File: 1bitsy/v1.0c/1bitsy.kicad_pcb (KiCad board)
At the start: 4 copper layers, 38.1 x 17.8 mm, 105 parts, among them J1 BOOT, P1 CONN_01X01, P10 CONN_01X01, P11 CONN_01X01, P12 CONN_01X01, P13 CONN_01X01, P14 CONN_01X01, P15 CONN_01X01, P16 CONN_01X01, P17 CONN_01X01, P18 CONN_01X01, P19 CONN_01X01, P2 CONN_01X01, P20 CONN_01X01, P21 CONN_01X01, P22 CONN_01X01, P23 CONN_01X01, P24 USB_OTG, P25 CONN_01X01, P26 CONN_01X01, P27 CONN_01X01, P28 CONN_01X01, P29 CONN_01X01, P3 CONN_01X01, P30 CONN_01X01, P31 CONN_01X01, P32 CONN_01X01, P33 CONN_01X01, P34 CONN_01X01, P35 CONN_01X01, P36 CONN_01X01, P37 CONN_01X01, P38 CONN_01X01, P39 CONN_01X01, P4 CONN_01X01, P40 CONN_01X01, P41 CONN_01X01, P42 CONN_01X01, P43 TP, P44 TP, P45 TP, P46 TP, P47 TP, P48 CONN_01X01, P49 CONN_01X01, P5 CONN_01X01, P50 CONN_01X01, P51 CONN_01X01, P52 CONN_01X01, P53 CONN_01X01, P54 CONN_01X01, P55 CONN_01X01, P6 CONN_01X01, P7 CONN_01X01, P8 CONN_01X01, P9 CONN_01X01, SW1 TACT_G, U1 VREG_3V3, U2 STM32F415RGT, X1 32.768kHz, X2 25MHz, X3 JTAG-10

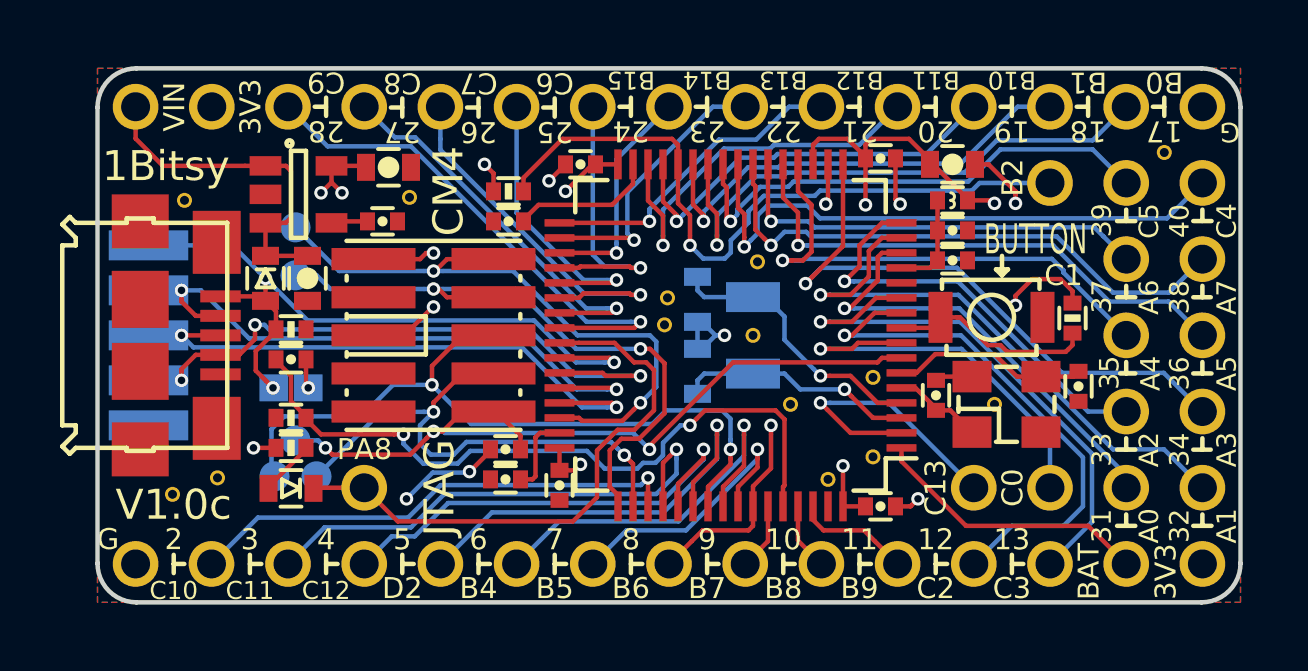
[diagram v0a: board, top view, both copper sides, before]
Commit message: More silkscreen polish.
Made the pixelheart larger, moved some via away from silkscreen lines.
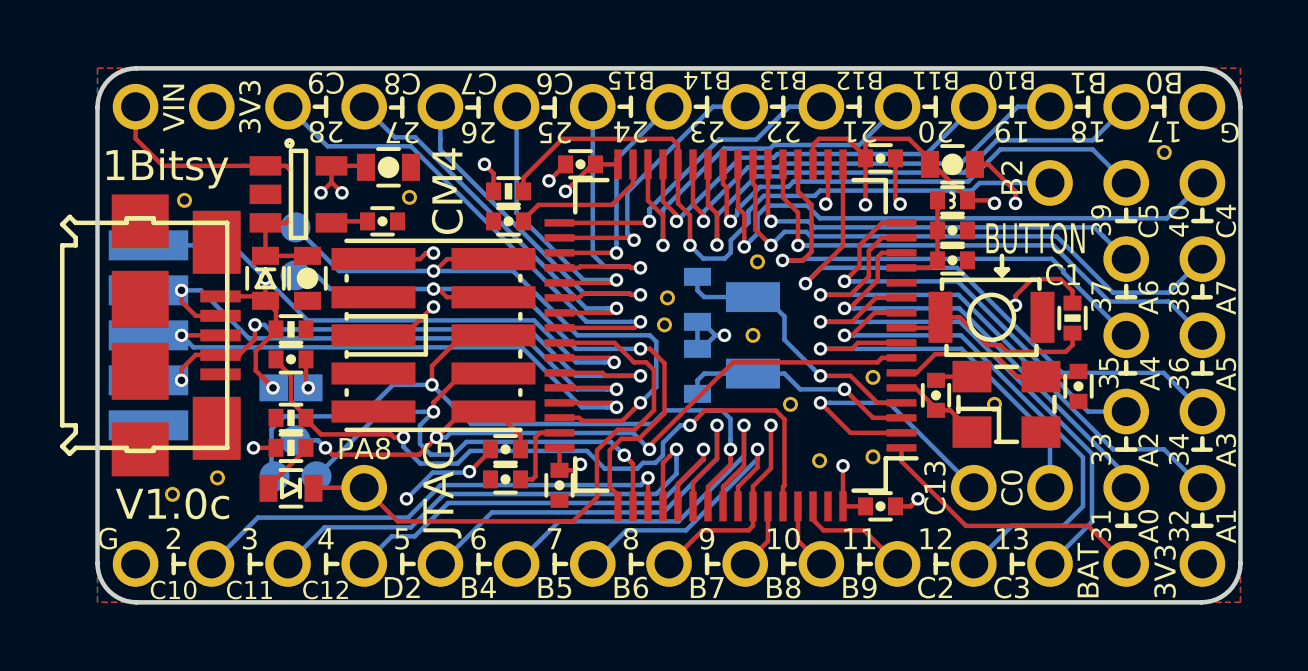
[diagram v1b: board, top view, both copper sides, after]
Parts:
- REF**: footprint pkl_logos:heart_mask_010grid -> pkl_logos:heart_mask_015grid
- moved REF** 0.76 mm to (130.0, 48.9)
- moved REF** 0.68 mm to (124.4, 49.9)

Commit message: Removed serial pin numbering, left only pin bank+pin no.
We got rid of the pcb specific numbering to make space for larger
internal mcu numbering labels. These are much more important when
writing code for the board.
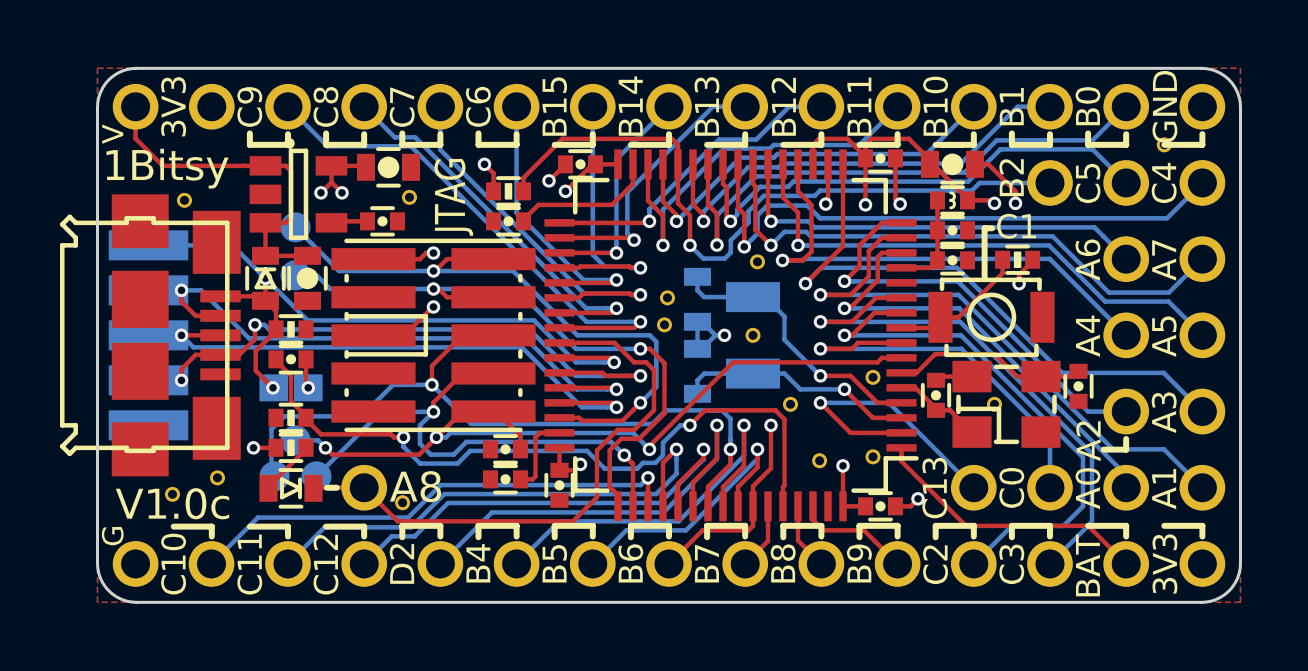
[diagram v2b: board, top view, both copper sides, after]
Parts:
- added REF**: via0305, pkl_misc:via0305, F.Cu at (110.5, 51.3)
- moved R5 2.67 mm to (131.0, 43.2), turned to 180 degrees
- moved REF** 0.78 mm to (127.1, 45.7)
- moved REF** 0.25 mm to (135.9, 39.4)
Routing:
- net GND: track 18.8 -> 15.3 mm, vias 10 -> 8
- net /BUTTON: track 6.81 -> 4.57 mm
- net +3V3: track 24.5 -> 22.5 mm
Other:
- board text added: "A8"
- board text added: "V"
- board text removed: "31"
- board text removed: "32"
- board text removed: "33"
- board text removed: "34"
- board text removed: "35"
- board text removed: "36"
- board text removed: "37"
- board text removed: "38"
- board text removed: "39"
- board text removed: "40"
- board text removed: "BUTTON"
- board text removed: "CM4"
- board text removed: "PA8"

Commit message: Some more Silkscreen cleanup work.
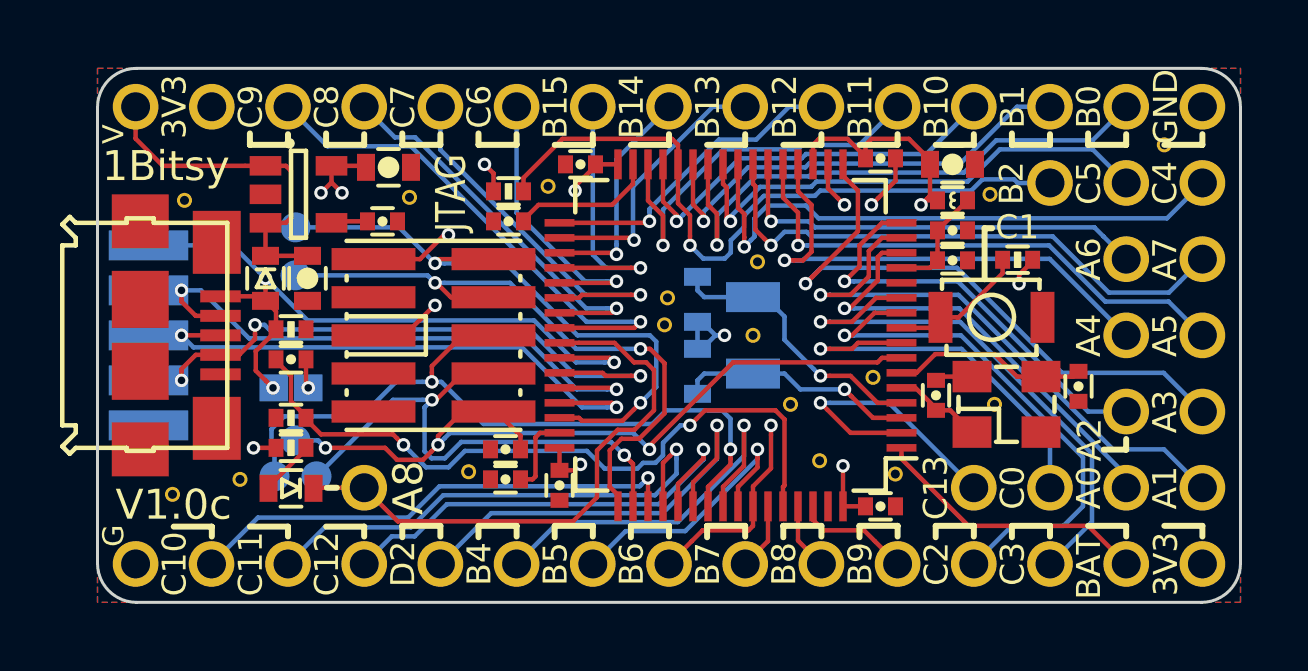
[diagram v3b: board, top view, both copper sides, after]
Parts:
- removed LOGO1: 1BitSquared, pkl_logos:1b2_Logo_SilkS_7.5mm
- added REF**: via0305, pkl_misc:via0305, F.Cu at (115.3, 40.8)
- added REF**: via0305, pkl_misc:via0305, F.Cu at (130.1, 41.0)
- added REF**: 1b2_Logo_SilkS_6.5mm, pkl_logos:1b2_Logo_SilkS_6.5mm, B.Cu at (111.9, 45.7)
- moved REF** 2.43 mm to (112.7, 50.3)
- moved REF** 0.94 mm to (126.9, 50.3)
- moved REF** 0.75 mm to (105.1, 50.5)
- moved REF** 0.30 mm to (129.7, 48.9)
- turned L1 to 0 degrees
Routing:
- net GND: track 15.3 -> 12.2 mm, vias 8 -> 5
- net +3V3: track 22.5 -> 20.8 mm, vias 10 -> 9
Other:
- board text added: "OSHPark"
- board text added: "with by"
- board text removed: "with by OSHPark"

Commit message: Swapped C4 & C5 for consistency.
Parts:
- moved P14 2.54 mm to (134.6, 40.6)
- moved P15 2.54 mm to (137.2, 40.6)
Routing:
- net /PC4: track 19.7 -> 17.2 mm
- net /PC5: track 16.7 -> 19.3 mm
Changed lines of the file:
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@@
     (thickness 1.6)
     (drawings 336)
-    (tracks 738)
+    (tracks 739)
     (zones 0)
     (modules 108)
@@
   )
   (module pkl_pin_headers:Pin_Header_Straight_Round_1x01 (layer F.Cu)
-    (at 137.16 40.64)
+    (at 134.62 40.64)
     (descr "Through hole pin header")
     (tags "pin header")
@@
   )
   (module pkl_pin_headers:Pin_Header_Straight_Round_1x01 (layer F.Cu)
-    (at 134.62 40.64 180)
+    (at 137.16 40.64 180)
     (descr "Through hole pin header")
     (tags "pin header")
@@
     (effects (font (size 0.8 0.8) (thickness 0.2)) (justify mirror))
   )
-  (gr_text C4 (at 135.9154 40.64 90) (layer B.SilkS)
+  (gr_text C4 (at 133.3754 40.64 90) (layer B.SilkS)
     (effects (font (size 0.8 0.8) (thickness 0.2)) (justify mirror))
   )
-  (gr_text C5 (at 133.3754 40.64 90) (layer B.SilkS)
+  (gr_text C5 (at 135.9408 40.64 90) (layer B.SilkS)
     (effects (font (size 0.8 0.8) (thickness 0.2)) (justify mirror))
   )
@@
     (effects (font (size 0.8 0.8) (thickness 0.2)))
   )
-  (gr_text C4 (at 135.9154 40.64 90) (layer F.SilkS)
+  (gr_text C4 (at 133.3754 40.64 90) (layer F.SilkS)
     (effects (font (size 0.8 0.8) (thickness 0.2)))
   )
-  (gr_text C5 (at 133.3754 40.64 90) (layer F.SilkS)
+  (gr_text C5 (at 135.9408 40.64 90) (layer F.SilkS)
     (effects (font (size 0.8 0.8) (thickness 0.2)))
   )
@@
   (segment (start 124.748198 45.27) (end 124.43 45.27) (width 0.15) (layer B.Cu) (net 27))
   (via (at 124.43 45.27) (size 0.45) (drill 0.25) (layers F.Cu B.Cu) (net 27))
-  (segment (start 137.16 40.64) (end 135.980999 41.819001) (width 0.15) (layer B.Cu) (net 28))
-  (segment (start 135.980999 41.819001) (end 124.364479 41.819001) (width 0.15) (layer B.Cu) (net 28))
-  (segment (start 124.364479 41.819001) (end 123.940478 41.395) (width 0.15) (layer B.Cu) (net 28))
-  (segment (start 123.940478 41.395) (end 122.655 41.395) (width 0.15) (layer B.Cu) (net 28))
-  (segment (start 122.655 41.395) (end 122.23 41.82) (width 0.15) (layer B.Cu) (net 28))
-  (segment (start 122.23 41.82) (end 122.23 42.429018) (width 0.15) (layer B.Cu) (net 28))
-  (segment (start 122.23 42.429018) (end 122.114017 42.545001) (width 0.15) (layer B.Cu) (net 28))
-  (segment (start 122.114017 42.545001) (end 121.889018 42.77) (width 0.15) (layer B.Cu) (net 28))
+  (segment (start 121.889018 42.77) (end 122.23 42.429018) (width 0.15) (layer B.Cu) (net 28))
+  (segment (start 122.23 42.429018) (end 122.23 41.82) (width 0.15) (layer B.Cu) (net 28))
+  (segment (start 122.23 41.82) (end 122.655 41.395) (width 0.15) (layer B.Cu) (net 28))
+  (segment (start 123.940478 41.395) (end 124.364479 41.819001) (width 0.15) (layer B.Cu) (net 28))
+  (segment (start 122.655 41.395) (end 123.940478 41.395) (width 0.15) (layer B.Cu) (net 28))
+  (segment (start 124.364479 41.819001) (end 133.440999 41.819001) (width 0.15) (layer B.Cu) (net 28))
+  (segment (start 133.440999 41.819001) (end 134.62 40.64) (width 0.15) (layer B.Cu) (net 28))
   (segment (start 121.889018 41.677814) (end 121.889018 42.451802) (width 0.15) (layer F.Cu) (net 28))
   (segment (start 121.68 41.468796) (end 121.889018 41.677814) (width 0.15) (layer F.Cu) (net 28))
@@
   (segment (start 121.68 40.02) (end 121.68 41.468796) (width 0.15) (layer F.Cu) (net 28))
   (via (at 121.889018 42.77) (size 0.45) (drill 0.25) (layers F.Cu B.Cu) (net 28))
-  (segment (start 129.332136 40.595) (end 124.29646 40.595) (width 0.15) (layer B.Cu) (net 29))
-  (segment (start 121.43 41.759746) (end 121.43 41.92) (width 0.15) (layer B.Cu) (net 29))
-  (segment (start 122.419746 40.77) (end 121.43 41.759746) (width 0.15) (layer B.Cu) (net 29))
-  (segment (start 124.12146 40.77) (end 122.419746 40.77) (width 0.15) (layer B.Cu) (net 29))
-  (segment (start 124.29646 40.595) (end 124.12146 40.77) (width 0.15) (layer B.Cu) (net 29))
-  (segment (start 133.5 39.52) (end 130.407136 39.52) (width 0.15) (layer B.Cu) (net 29))
-  (segment (start 134.62 40.64) (end 133.5 39.52) (width 0.15) (layer B.Cu) (net 29))
-  (segment (start 130.407136 39.52) (end 129.332136 40.595) (width 0.15) (layer B.Cu) (net 29))
+  (segment (start 121.43 41.92) (end 121.43 41.759746) (width 0.15) (layer B.Cu) (net 29))
+  (segment (start 121.43 41.759746) (end 122.419746 40.77) (width 0.15) (layer B.Cu) (net 29))
+  (segment (start 122.419746 40.77) (end 124.12146 40.77) (width 0.15) (layer B.Cu) (net 29))
+  (segment (start 124.12146 40.77) (end 124.29646 40.595) (width 0.15) (layer B.Cu) (net 29))
+  (segment (start 129.332136 40.595) (end 130.407136 39.52) (width 0.15) (layer B.Cu) (net 29))
+  (segment (start 124.29646 40.595) (end 129.332136 40.595) (width 0.15) (layer B.Cu) (net 29))
+  (segment (start 130.407136 39.52) (end 135.23 39.52) (width 0.15) (layer B.Cu) (net 29))
+  (segment (start 135.23 39.52) (end 136.33 40.62) (width 0.15) (layer B.Cu) (net 29))
+  (segment (start 136.33 40.62) (end 137.14 40.62) (width 0.15) (layer B.Cu) (net 29))
+  (segment (start 137.14 40.62) (end 137.16 40.64) (width 0.15) (layer B.Cu) (net 29))
   (via (at 121.43 41.92) (size 0.45) (drill 0.25) (layers F.Cu B.Cu) (net 29))
   (segment (start 121.305001 41.795001) (end 121.43 41.92) (width 0.15) (layer F.Cu) (net 29))

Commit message: Updated Fab legend.
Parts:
- L1: value 600 Ferrite -> Ferr

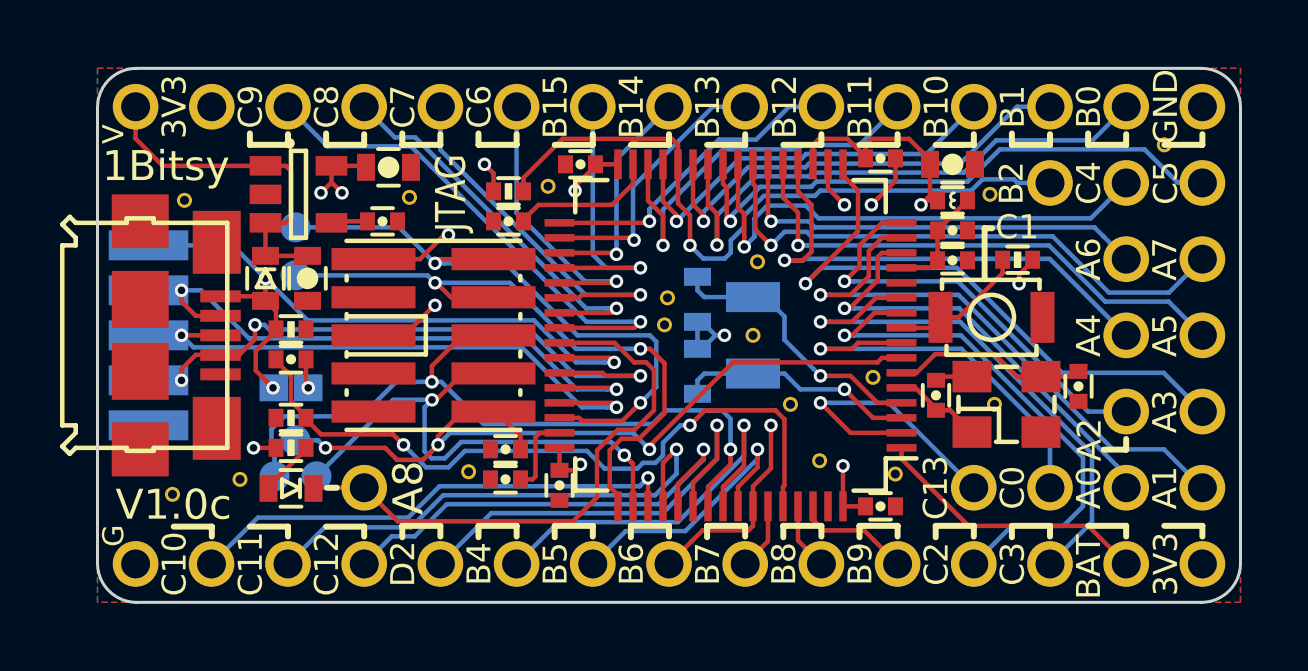
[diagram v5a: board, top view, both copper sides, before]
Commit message: Recovered v1.0c pcb revision, added v1.0d.
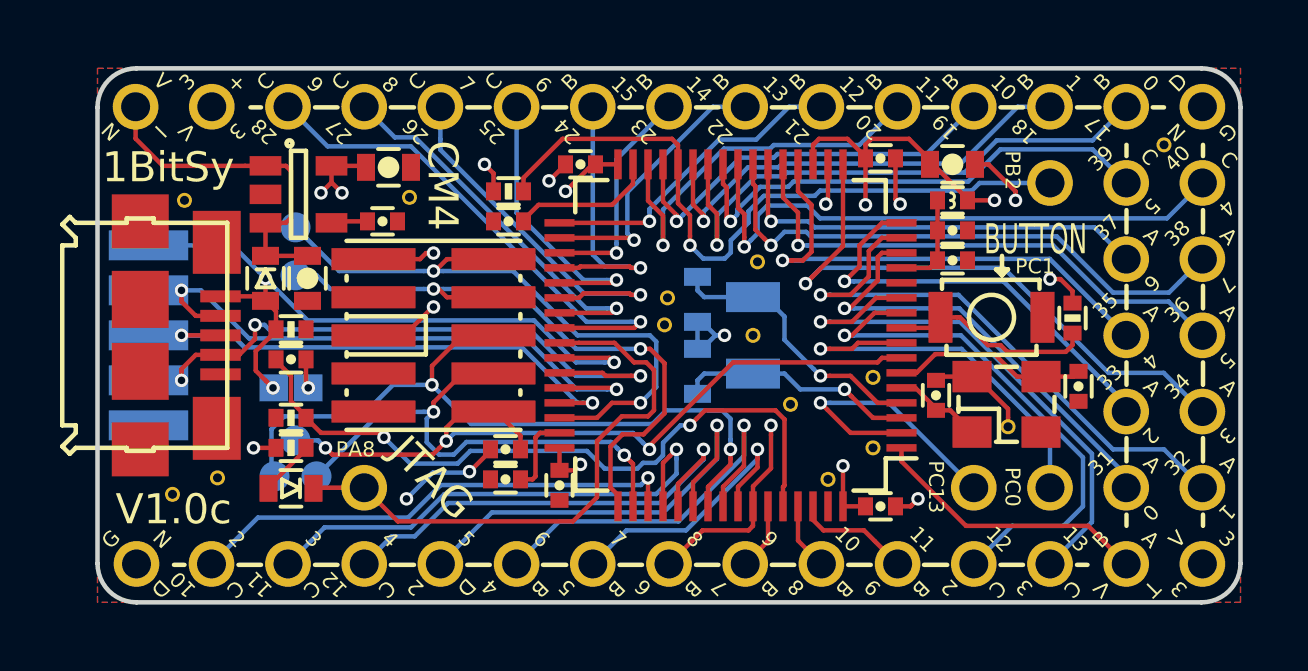
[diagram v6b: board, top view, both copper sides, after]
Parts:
- removed the REF** at (115.3, 40.8)
- removed the REF** at (127.1, 45.7)
- removed the REF** at (129.7, 48.9)
- removed the REF** at (130.1, 41.0)
- removed the REF** at (111.9, 45.7)
- removed the REF** at (112.7, 50.3)
- added LOGO1: 1BitSquared, pkl_logos:1b2_Logo_SilkS_7.5mm, B.Cu at (113.5, 45.7)
- L1: value Ferr -> 600 Ferrite
- moved R5 2.67 mm to (132.8, 45.1), turned to 270 degrees
- moved P14 2.54 mm to (137.2, 40.6)
- moved P15 2.54 mm to (134.6, 40.6)
- moved REF** 1.15 mm to (126.2, 49.5)
- moved REF** 0.87 mm to (130.7, 48.8)
- moved REF** 0.75 mm to (104.3, 50.5)
- moved REF** 0.68 mm to (124.7, 50.5)
- turned L1 to 180 degrees
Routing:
- net GND: track 12.2 -> 20.8 mm, vias 5 -> 10
- net /PC4: track 17.2 -> 19.7 mm
- net /PC5: track 19.3 -> 16.7 mm
- net /BUTTON: track 4.57 -> 6.81 mm
- net +3V3: track 20.8 -> 22.7 mm, vias 9 -> 10
- net /USB_D+: track 18.8 -> 17.0 mm
- net /JTAG_TDI: track 18.1 -> 17.5 mm
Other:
- board text added: "+"
- board text added: "0"
- board text added: "1BitSy"
- board text added: "1BitSy V1.0c STM32 F4x5RGT6"
- board text added: "31"
- board text added: "32"
- board text added: "33"
- board text added: "34"
- board text added: "35"
- board text added: "36"
- board text added: "37"
- board text added: "38"
- board text added: "39"
- board text added: "40"
- board text added: "A"
- board text added: "B"
- board text added: "BUTTON"
- board text added: "C"
- board text added: "CM4"
- board text added: "D"
- board text added: "I"
- board text added: "N"
- board text added: "PA8"
- board text added: "PB2"
- board text added: "PC0"
- board text added: "PC1"
- board text added: "PC13"
- board text added: "T"
- board text removed: "1Bitsy"
- board text removed: "A0"
- board text removed: "A1"
- board text removed: "A2"
- board text removed: "A3"
- board text removed: "A4"
- board text removed: "A5"
- board text removed: "A6"
- board text removed: "A7"
- board text removed: "A8"
- board text removed: "B0"
- board text removed: "B1"
- board text removed: "B10"
- board text removed: "B11"
- board text removed: "B12"
- board text removed: "B13"
- board text removed: "B14"
- board text removed: "B15"
- board text removed: "B2"
- board text removed: "B4"
- board text removed: "B5"
- board text removed: "B6"
- board text removed: "B7"
- board text removed: "B8"
- board text removed: "B9"
- board text removed: "BAT"
- board text removed: "C0"
- board text removed: "C1"
- board text removed: "C10"
- board text removed: "C11"
- board text removed: "C12"
- board text removed: "C13"
- board text removed: "C2"
- board text removed: "C3"
- board text removed: "C4"
- board text removed: "C5"
- board text removed: "C6"
- board text removed: "C7"
- board text removed: "C8"
- board text removed: "C9"
- board text removed: "D2"
- board text removed: "OSHPark"
- board text removed: "with by"

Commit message: Added 1Bitsy logo. Improved back side silkscreen.
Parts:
- added REF**: heart_mask_010grid, pkl_logos:heart_mask_010grid, B.Cu at (130.7, 49.0)
- added REF**: 1bitsy_copper_025grid, pkl_logos:1bitsy_silk_025grid, B.Cu at (131.8, 45.7)
- moved REF** 0.87 mm to (130.2, 48.0)
- moved REF** 0.30 mm to (126.2, 49.8)
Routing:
- net GND: track 20.8 -> 18.7 mm
- net +3V3: track 22.7 -> 24.4 mm
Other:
- board text added: "with by OSHPark"
- board text removed: "1BitSy V1.0c STM32 F4x5RGT6"
